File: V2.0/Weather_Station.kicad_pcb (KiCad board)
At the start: 4 copper layers, 41 parts, among them J1 HS91L02W2C01, J2 TYPE-C16PIN, J3 B-2100S04P-A110, J4 B-2100S04P-A110, J5 ZX-PZ2.54-1-6PZZ, U1 STM32F103C8T6, U2 HDC1080DMBR, U3 AMS1117-3.3, U5 SRV05-4, Y1 X322516MLB4SI

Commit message: Progressed with much more cleaner design.
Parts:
- J1: moved to B.Cu
- moved F1 102.8 mm to (205.5, 90.5)
- moved J2 102.5 mm to (213.0, 86.0), turned to 90 degrees
- moved R4 97.5 mm to (205.0, 82.5), turned to -90 degrees
- moved R9 96.3 mm to (206.8, 82.5), turned to -90 degrees
- moved R5 95.1 mm to (203.2, 82.5), turned to 90 degrees
- moved R7 92.6 mm to (190.5, 98.8), turned to -90 degrees
- moved U3 92.1 mm to (201.2, 95.2), turned to 180 degrees
- moved R6 90.5 mm to (192.2, 98.8), turned to -90 degrees
- moved R8 89.7 mm to (188.8, 98.8), turned to -90 degrees
- moved R12 89.0 mm to (199.2, 89.0), turned to -90 degrees
- moved R10 88.1 mm to (197.5, 85.8), turned to 90 degrees
- moved R11 85.5 mm to (195.8, 85.8), turned to 90 degrees
- moved U5 84.3 mm to (205.5, 86.5), turned to 180 degrees
- moved C21 84.1 mm to (177.8, 100.8), turned to 90 degrees
- moved C22 83.6 mm to (207.0, 95.2), turned to -90 degrees
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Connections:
- net Net-(J2-SHIELD) renamed /Shield
- U1 pad 13: unconnected-(U1-PA3-Pad13) -> /LED_B
- U1 pad 17: unconnected-(U1-PA7-Pad17) -> /LED_W
- U1 pad 18: /RTC_CLK -> unconnected-(U1-PB0-Pad18)
- U1 pad 19: /RTC_INT -> unconnected-(U1-PB1-Pad19)
- U1 pad 2: /LED_B -> unconnected-(U1-PC13-Pad2)
- U1 pad 20: unconnected-(U1-PB2-Pad20) -> /LED_R
- U1 pad 3: /LED_R -> unconnected-(U1-PC14-Pad3)
- U1 pad 4: /LED_W -> unconnected-(U1-PC15-Pad4)
- U1 pad 40: unconnected-(U1-PB4-Pad40) -> /RTC_INT
- U1 pad 41: unconnected-(U1-PB5-Pad41) -> /RTC_CLK
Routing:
- net /USB_D-: track 0.00 -> 17.2 mm
- net /USB_D+: track 0.00 -> 17.2 mm

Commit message: Made Progress with Design of V2.
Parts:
- moved C10 5.88 mm to (187.0, 98.8)
- moved D3 4.32 mm to (184.5, 101.2), turned to 0 degrees
- moved R1 3.50 mm to (195.8, 85.8)
- moved R11 3.50 mm to (199.2, 85.8)
- moved D1 2.61 mm to (188.0, 101.2), turned to 0 degrees
- moved C8 2.02 mm to (182.0, 95.8)
- moved C9 2.02 mm to (182.0, 98.8)
- moved FB1 2.02 mm to (184.8, 97.2)
- moved R5 2.02 mm to (205.2, 82.2)
- moved R4 1.52 mm to (203.5, 82.2)
- moved D2 1.06 mm to (191.5, 101.2), turned to 0 degrees
- moved C21 1.00 mm to (177.8, 99.8)
- moved U2 1.00 mm to (175.1, 99.8)
- moved J4 0.53 mm to (191.9, 82.2)
- moved R9 0.35 mm to (207.0, 82.2)
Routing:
- net /I2C1_SCL: track 0.00 -> 50.4 mm, vias 0 -> 2
- net /I2C1_SDA: track 0.00 -> 48.7 mm, vias 0 -> 1
- net +3.3V: track 0.00 -> 23.3 mm
- net /USART1_TX: track 0.00 -> 13.3 mm, vias 0 -> 1
- net /CC1: track 0.00 -> 12.7 mm, vias 0 -> 2
- net /USART1_RX: track 0.00 -> 11.1 mm, vias 0 -> 1
- net /RTC_CLK: track 0.00 -> 10.9 mm, vias 0 -> 1
- net /VBUS_IN: track 0.00 -> 10.1 mm, vias 0 -> 2
- net /OSC_IN: track 0.00 -> 9.44 mm
- net /RTC_INT: track 0.00 -> 8.89 mm, vias 0 -> 1
- net /NRST: track 0.00 -> 7.51 mm
- net +3.3VA: track 0.00 -> 7.46 mm
- net /OSC_OUT: track 0.00 -> 6.84 mm
- net GND: track 0.00 -> 6.60 mm
- net Net-(D3-A): track 0.00 -> 4.69 mm
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
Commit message: Nearly finished V2.
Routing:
- net +3.3V: track 23.3 -> 78.9 mm, vias 0 -> 5
- net VBUS: track 0.00 -> 47.0 mm, vias 0 -> 3
- net GND: track 6.60 -> 36.8 mm, vias 0 -> 63
- net /Shield: track 0.00 -> 20.5 mm
- net /BOOT0: track 0.00 -> 9.13 mm, vias 0 -> 2
- net /uC_SWDIO: track 0.00 -> 7.64 mm
- net /uC_SWCLK: track 0.00 -> 3.92 mm
- net /SWCLK: track 0.00 -> 2.87 mm
- net /SWDIO: track 0.00 -> 2.81 mm
- net /USB_D+: track 17.2 -> 19.9 mm
- net /USB_D-: track 17.2 -> 19.6 mm
- net /I2C1_SDA: track 48.7 -> 50.5 mm
- net /I2C1_SCL: track 50.4 -> 51.6 mm
- net /RTC_CLK: track 10.9 -> 11.5 mm
- net /RTC_INT: track 8.89 -> 9.48 mm
- added copper zone on F.Cu, net +3.3V
- added copper zone on B.Cu, net GND
- added copper zone on F.Cu, net GND
- added copper zone on In1.Cu, net GND
- added copper zone on In2.Cu, net GND
- added copper zone on F.Cu, net VBUS
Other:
- board outline added: 44.8 x 24 mm

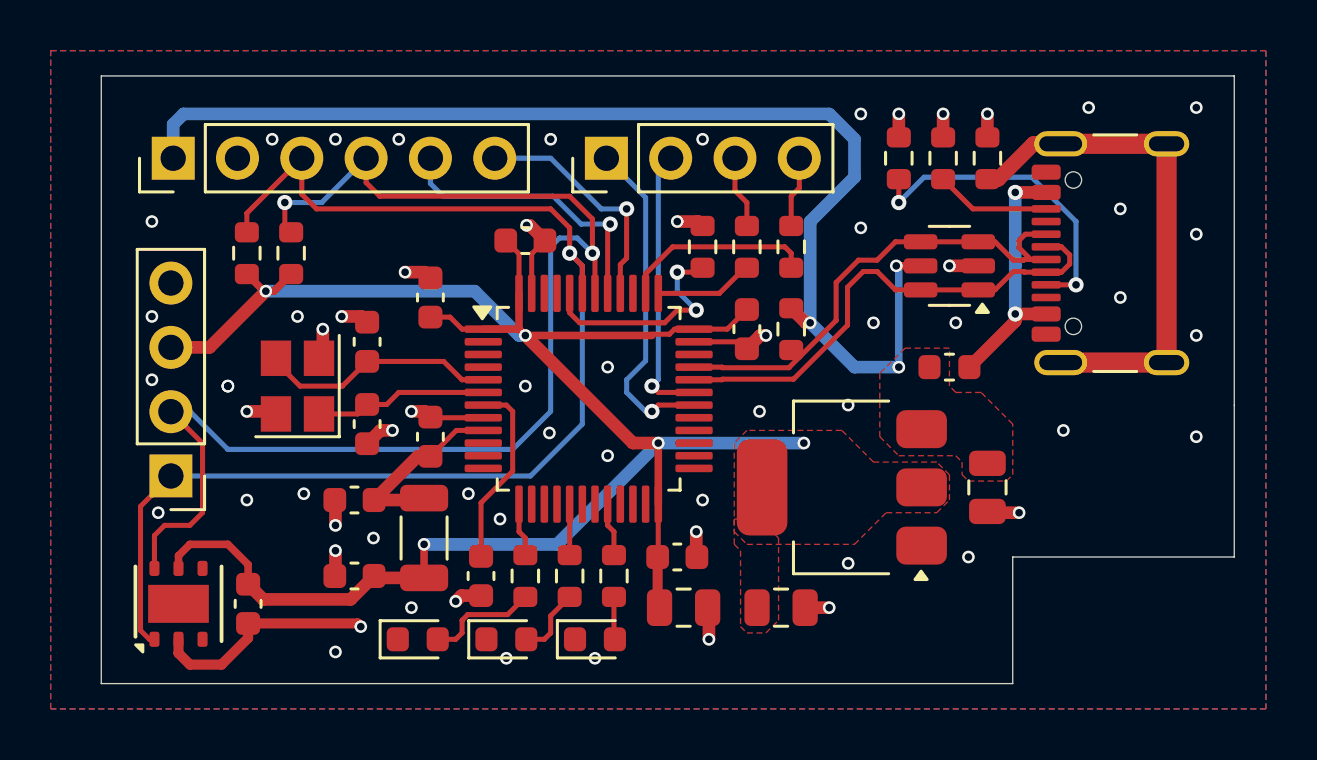
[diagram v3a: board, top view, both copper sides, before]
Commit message: V2 nerly finished. Round corners / DRC need to be done.
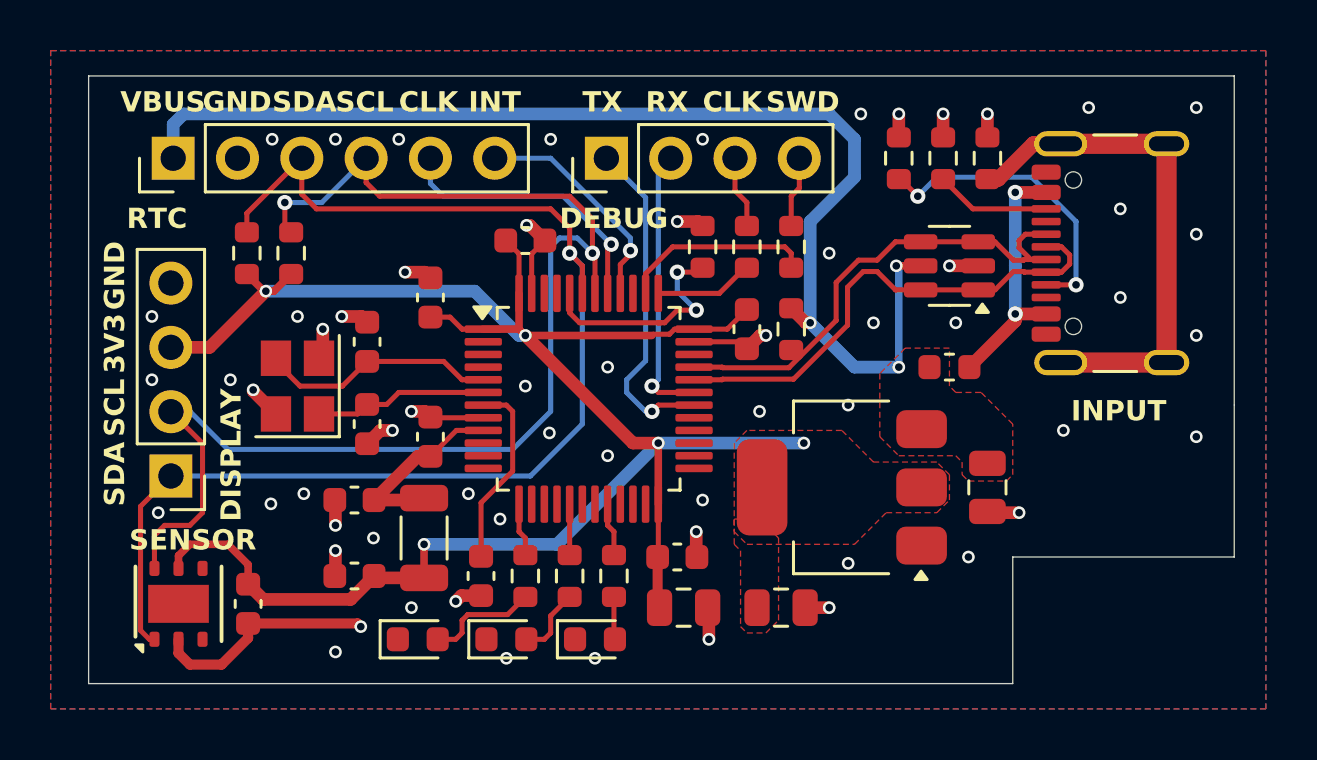
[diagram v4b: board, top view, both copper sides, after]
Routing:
- net /CC1: track 12.7 -> 12.0 mm
- net GND: track 36.8 -> 36.9 mm, vias 63 -> 61
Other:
- board size 44.8 x 24 mm -> 45.2 x 24 mm
- board text added: "3V3"
- board text added: "CLK"
- board text added: "DEBUG"
- board text added: "DISPLAY"
- board text added: "GND"
- board text added: "INPUT"
- board text added: "INT"
- board text added: "RTC"
- board text added: "RX"
- board text added: "SCL"
- board text added: "SDA"
- board text added: "SENSOR"
- board text added: "SWD"
- board text added: "TX"
- board text added: "VBUS"

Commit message: V2 should be finished!!
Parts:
- added G***: LOGO, LOGO, B.Cu at (206.1, 100.5)
- J3: moved to B.Cu
- moved R4 1.20 mm to (202.3, 82.2)
- moved R5 1.20 mm to (204.1, 82.2)
- moved R9 1.20 mm to (205.8, 82.2)
- turned J3 to 0 degrees
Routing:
- net /CC1: track 12.0 -> 15.0 mm
- net /CC2: track 4.56 -> 6.21 mm
- net /Shield: track 20.5 -> 21.7 mm
- net GND: track 36.9 -> 37.0 mm, vias 61 -> 65
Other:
- outline, holes or cut-outs redrawn
- board text added: "Weather Station V2.0"

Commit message: This is ordered Version of Weather Station V2!!!
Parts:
- FB1: footprint Inductor_SMD:L_1206_3216Metric -> Inductor_SMD:L_0603_1608Metric
- moved C9 1.44 mm to (182.5, 97.4)
- moved FB1 0.79 mm to (185.0, 96.5)
- moved C8 0.50 mm to (182.5, 95.8)
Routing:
- net +3.3V: track 78.9 -> 80.8 mm
- net +3.3VA: track 7.46 -> 5.94 mm
- net GND: track 37.0 -> 37.1 mm, vias 65 -> 67
- net (no net): vias 0 -> 2
